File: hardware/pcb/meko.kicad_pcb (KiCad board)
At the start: 2 copper layers, 204 parts, among them IC1 MCP16502AB, IC2 MAYA-W386-00B, IC3 TAC5212, J1 Micro_SD_Card_Det1, J2 Micro_SD_Card_Det1, J3 USB_C_Receptacle_USB2.0_16P, J4 Conn_ARM_JTAG_SWD_10, J5 503480-1000, J6 PJ-342, J7 PJ-242, SW10 SW_Push, SW6 SW_Push, SW7 SW_Push, SW8 SW_Push, SW9 SW_Push, U1 SAMA7D65-4HB, U3 MAX17260, U4 BQ25640, U5 ECMF02-2AMX6, U6 TPS7A2033PDBV, U7 DRV2605LDGS, U8 MT41K256M16TW, Y1 32kHz768, Y2 24MHz, Y3 32kHz768

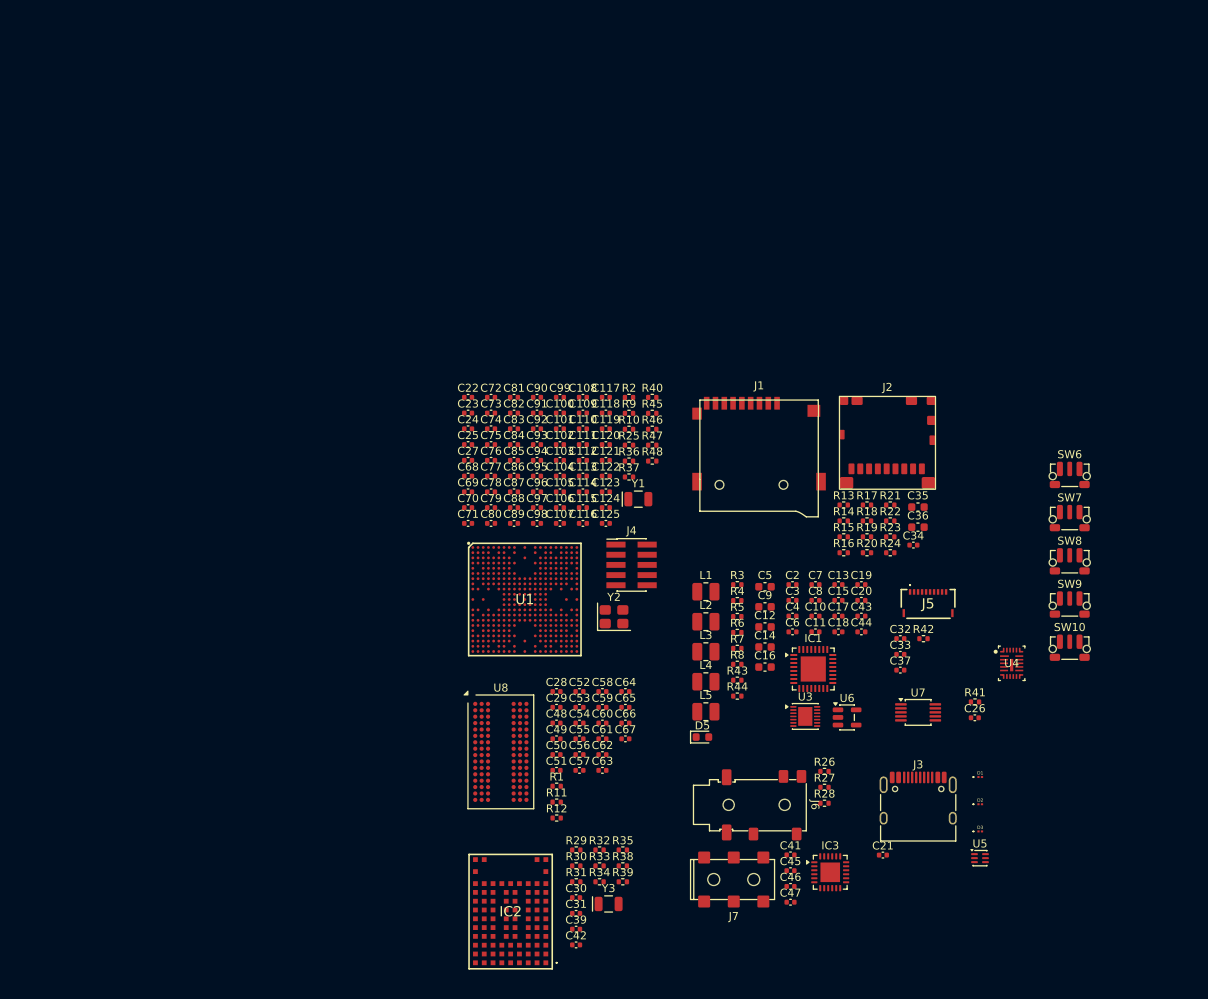
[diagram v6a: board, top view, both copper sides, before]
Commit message: mainboard: deleted footprint from pcb
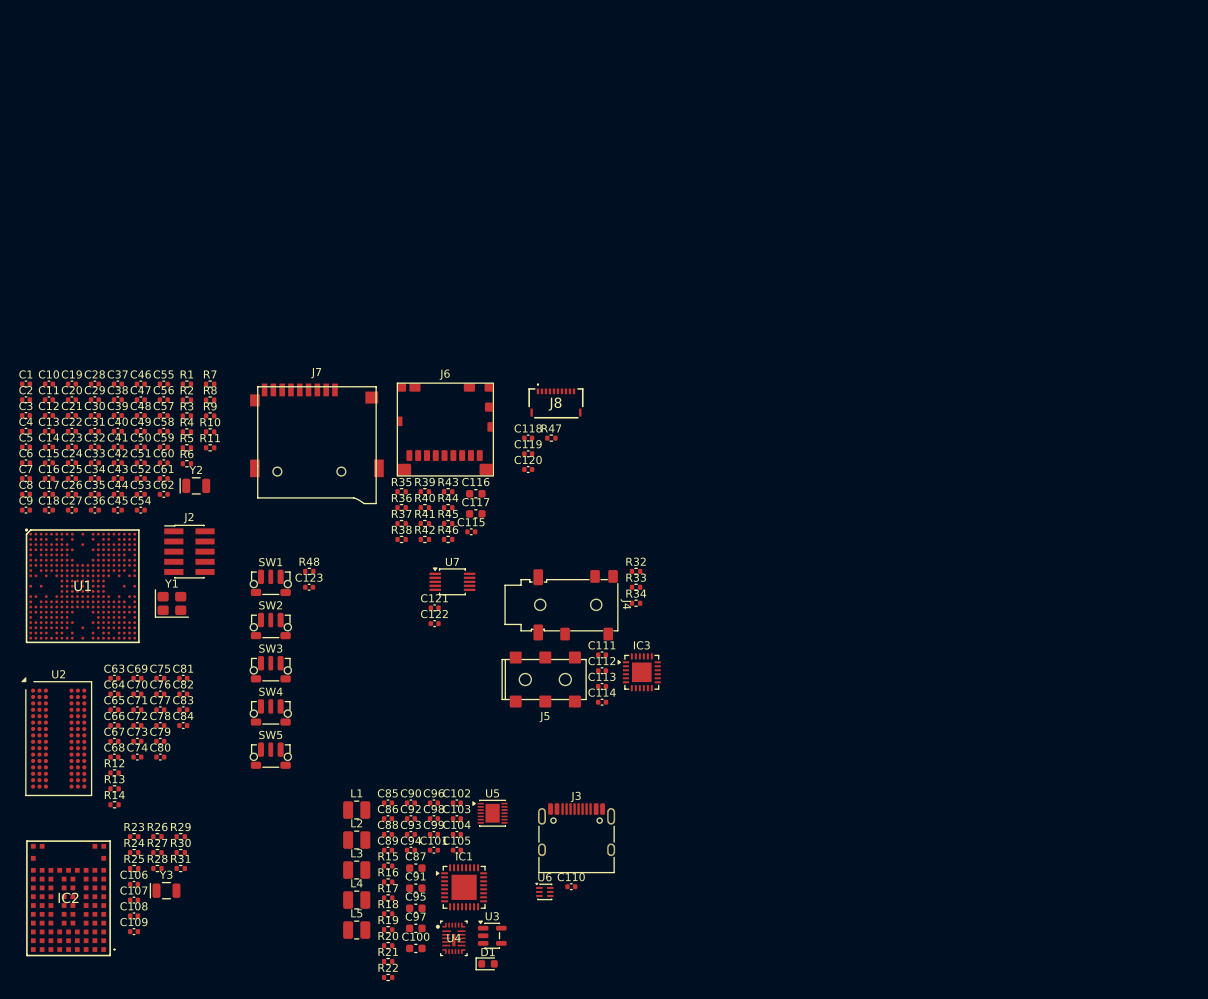
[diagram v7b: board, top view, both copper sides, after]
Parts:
- removed C124, C125: 100n, Capacitor_SMD:C_0402_1005Metric
- removed D2, D3: ESD441, ESD441DPLR:ESD441DPLR
- removed D5: LED, LED_SMD:LED_0603_1608Metric
- removed J1: Micro_SD_Card_Det1, PCM_ckl-connector:microSD_XYECONN_TF-015-ZYD9AH185
- removed SW10, SW6, SW7, SW8, SW9: SW_Push, Button_Switch_SMD:SW_Push_1P1T-MP_NO_Horizontal_Alps_SKRTLAE010
- removed U8: MT41K256M16TW, Package_BGA:Micron_FBGA-96_8x14mm_Layout9x16_P0.8mm
- added C1: 9p, Capacitor_SMD:C_0402_1005Metric, F.Cu at (14.6, 66.5)
- added C38: 100n, Capacitor_SMD:C_0402_1005Metric, F.Cu at (26.1, 68.5)
- added C40: 100n, Capacitor_SMD:C_0402_1005Metric, F.Cu at (26.1, 72.4)
- added J8: 503480-1000, 503480-1000:5034801000, F.Cu at (80.8, 68.9)
- added SW1: SW_Push, Button_Switch_SMD:SW_Push_1P1T-MP_NO_Horizontal_Alps_SKRTLAE010, F.Cu at (45.2, 91.5)
- added SW2: SW_Push, Button_Switch_SMD:SW_Push_1P1T-MP_NO_Horizontal_Alps_SKRTLAE010, F.Cu at (45.2, 96.9)
- added SW3: SW_Push, Button_Switch_SMD:SW_Push_1P1T-MP_NO_Horizontal_Alps_SKRTLAE010, F.Cu at (45.2, 102.3)
- added SW4: SW_Push, Button_Switch_SMD:SW_Push_1P1T-MP_NO_Horizontal_Alps_SKRTLAE010, F.Cu at (45.2, 107.7)
- added SW5: SW_Push, Button_Switch_SMD:SW_Push_1P1T-MP_NO_Horizontal_Alps_SKRTLAE010, F.Cu at (45.2, 113.1)
- added U2: MT41K256M16TW, Package_BGA:Micron_FBGA-96_8x14mm_Layout9x16_P0.8mm, F.Cu at (18.7, 110.8)
- C100: value 4u7 -> 22u; footprint Capacitor_SMD:C_0402_1005Metric -> Capacitor_SMD:C_0603_1608Metric
- C101, C103, C104, C105, C52, C53, C64, C66, C8, C93, C94, C96, C98: value 100n -> 4u7
- C102: value 100n -> 470n
- C106, C107, C110, C111, C112, C120, C121, C122, C85: value 100n -> 1u
- C108, C109: value 100n -> 9p
- C11, C13, C15, C17, C18, C19, C48, C67, C68, C83: value 4u7 -> 100n
- C113, C114, C86, C88: value 100n -> 10u
- C115: value 4u7 -> 10u
- C116, C117, C87, C91, C95, C97: value 100n -> 22u; footprint Capacitor_SMD:C_0402_1005Metric -> Capacitor_SMD:C_0603_1608Metric
- C119, C89, C90: value 4u7 -> 1u
- C12, C14, C16, C35, C36: value 22u -> 100n; footprint Capacitor_SMD:C_0603_1608Metric -> Capacitor_SMD:C_0402_1005Metric
- C2: value 1u -> 21pF
- C20, C34, C45, C46: value 10u -> 100n
- C21, C32, C37, C39, C41, C42, C43, C44, C47: value 1u -> 100n
- C22, C23, C27, C30, C31: value 9p -> 100n
- C24, C25: value 21pF -> 100n
- C3: value 10u -> 21pF
- C4: value 47n -> 100n
- C5: value 22u -> 9p; footprint Capacitor_SMD:C_0603_1608Metric -> Capacitor_SMD:C_0402_1005Metric
- C6: value 4u7 -> 9p
- C7: value 470n -> 4u7
- C9: value 22u -> 4u7; footprint Capacitor_SMD:C_0603_1608Metric -> Capacitor_SMD:C_0402_1005Metric
- C92: value 100n -> 47n
- D1: value ESD441 -> LED; footprint ESD441DPLR:ESD441DPLR -> LED_SMD:LED_0603_1608Metric
- J2: value Micro_SD_Card_Det1 -> Conn_ARM_JTAG_SWD_10; footprint PCM_ckl-connector:microSD_SOFNG_TF-008 -> Connector_PinHeader_1.27mm:PinHeader_2x05_P1.27mm_Vertical_SMD
- J4: value Conn_ARM_JTAG_SWD_10 -> PJ-342; footprint Connector_PinHeader_1.27mm:PinHeader_2x05_P1.27mm_Vertical_SMD -> PCM_ckl-connector:Jack_3.5mm_SHOUHAN_PJ-342
- J5: value 503480-1000 -> PJ-242; footprint 503480-1000:5034801000 -> PJ242:Jack_2.5mm_PJ242_6P_12x6.2x4mm_Horizontal
- J6: value PJ-342 -> Micro_SD_Card_Det1; footprint PCM_ckl-connector:Jack_3.5mm_SHOUHAN_PJ-342 -> PCM_ckl-connector:microSD_SOFNG_TF-008
- J7: value PJ-242 -> Micro_SD_Card_Det1; footprint PJ242:Jack_2.5mm_PJ242_6P_12x6.2x4mm_Horizontal -> PCM_ckl-connector:microSD_XYECONN_TF-015-ZYD9AH185
- R1, R2: value 240R -> 10k
- R10: value 4k02 -> 16k9
- R11: value 1k -> 16k9
- R13, R32: value 47k -> 1k
- R14: value 47k -> 240R
- R15, R16, R17, R21, R23, R30, R31: value 47k -> 10k
- R19: value 47k -> 1k5
- R20: value 47k -> 100R
- R22: value 47k -> 10m
- R25, R35, R36, R37, R38, R39, R41, R42, R43, R44: value 10k -> 47k
- R26, R27: value 100k -> 47k
- R28: value 1k -> 47k
- R3: value 100R -> 240R
- R33: value 47k -> 100k
- R34: value 10k -> 100k
- R4: value 10m -> 10k
- R45: value 16k9 -> 47k
- R46, R47, R48: value 16k9 -> 10k
- R5: value 1k5 -> 10k
- R6: value 10k -> 5k62
- R7: value 10k -> 4k02
- R8: value 10k -> 16k9
- R9: value 5k62 -> 16k9
- U3: value MAX17260 -> TPS7A2033PDBV; footprint Package_DFN_QFN:TDFN-14-1EP_3x3mm_P0.4mm_EP1.78x2.35mm -> Package_TO_SOT_SMD:SOT-23-5
- U5: value ECMF02-2AMX6 -> MAX17260; footprint Package_DFN_QFN:ST_UQFN-6L_1.5x1.7mm_P0.5mm -> Package_DFN_QFN:TDFN-14-1EP_3x3mm_P0.4mm_EP1.78x2.35mm
- U6: value TPS7A2033PDBV -> ECMF02-2AMX6; footprint Package_TO_SOT_SMD:SOT-23-5 -> Package_DFN_QFN:ST_UQFN-6L_1.5x1.7mm_P0.5mm
- Y1: value 32kHz768 -> 24MHz; footprint Crystal:Crystal_SMD_MicroCrystal_CC7V-T1A-2Pin_3.2x1.5mm -> Crystal:Crystal_SMD_3225-4Pin_3.2x2.5mm
- Y2: value 24MHz -> 32kHz768; footprint Crystal:Crystal_SMD_3225-4Pin_3.2x2.5mm -> Crystal:Crystal_SMD_MicroCrystal_CC7V-T1A-2Pin_3.2x1.5mm
- moved C26 116.3 mm to (20.3, 80.3)
- moved C21 115.3 mm to (20.3, 70.5)
- moved C37 104.1 mm to (26.1, 66.5)
- moved C32 103.5 mm to (23.2, 74.4)
- moved C33 103.5 mm to (23.2, 76.4)
- moved C36 102.9 mm to (23.2, 82.3)
- moved C35 102.9 mm to (23.2, 80.3)
- moved C46 102.7 mm to (28.9, 66.5)
- moved C47 102.7 mm to (28.9, 68.5)
- moved C34 102.7 mm to (23.2, 78.3)
- moved C20 101.8 mm to (20.3, 68.5)
- moved C19 101.8 mm to (20.3, 66.5)
- moved R23 101.7 mm to (28.1, 123.1)
- moved R24 101.7 mm to (28.1, 125.1)
- moved C13 100.5 mm to (17.5, 72.4)
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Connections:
- net /Touch Pad/SCL renamed /Touchpad/SCL
- net /Touch Pad/SDA renamed /Touchpad/SDA
- C10 pad 1: +VSYS -> +1V35_DDR
- C100 pad 1: +1V35_DDR -> +1V15_CPU
- C101 pad 1: +1V35_DDR -> +VSYS
- C102 pad 1: +1V35_DDR -> Net-(U5-REG)
- C103 pad 1: +1V35_DDR -> +VSYS
- C104 pad 1: +1V35_DDR -> +1V8_BATT_CPU
- C105 pad 1: +1V35_DDR -> +1V8
- C106 pad 1: +1V35_DDR -> GND
- C106 pad 2: GND -> +1V8
- C107 pad 1: +1V35_DDR -> +3V3
- C108 pad 1: +1V35_DDR -> Net-(IC2-SLP_XTAL_OUT)
- C109 pad 1: +1V35_DDR -> Net-(IC2-SLP_XTAL_IN)
- C11 pad 1: +VSYS -> +1V15_CORE
- C110 pad 1: +1V35_DDR -> GND
- C110 pad 2: GND -> VBUS
- C111 pad 1: +1V35_DDR -> GND
- C111 pad 2: GND -> Net-(IC3-DREG)
- C112 pad 1: +1V35_DDR -> GND
- C112 pad 2: GND -> Net-(IC3-VREF)
- C113 pad 1: +1V35_DDR -> GND
- C113 pad 2: GND -> +3V3
- C114 pad 1: +1V35_DDR -> GND
- C114 pad 2: GND -> +3V3_AVDD
- C115 pad 1: +1V8 -> +3V3
- C116 pad 1: +1V8 -> +3V3
- C117 pad 1: +1V8 -> +3V3
- C118 pad 1: +1V8 -> GND
- C118 pad 2: GND -> /Display/DISP
- C119 pad 1: +2V5 -> GND
- C119 pad 2: GND -> +3V3
- C12 pad 1: +1V35_DDR -> +1V15_CPU
- C120 pad 1: +2V5 -> GND
- C120 pad 2: GND -> +3V3
- C121 pad 1: +2V5 -> GND
- C121 pad 2: GND -> +3V3
- C122 pad 1: +2V5 -> GND
- C122 pad 2: GND -> Net-(U7-REG)
- C123 pad 1: +2V5 -> GND
- C123 pad 2: GND -> /Buttons/PWR
- C13 pad 1: +VSYS -> +3V3
- C14 pad 1: +1V15_CORE -> +1V35_DDR
- C15 pad 1: +VSYS -> +1V15_CORE
- C17 pad 1: +VSYS -> +3V3
- C18 pad 1: +1V8_BATT_CPU -> +1V35_DDR
- C19 pad 1: +1V8 -> +1V15_CORE
- C2 pad 1: VBUS -> Net-(U1SYS-XIN)
- C20 pad 1: +VSYS -> +1V15_CPU
- C21 pad 1: GND -> +3V3
- C21 pad 2: VBUS -> GND
- C22 pad 1: Net-(U1SYS-XIN32) -> +1V35_DDR
- C23 pad 1: Net-(U1SYS-XOUT32) -> +1V15_CORE
- C24 pad 1: Net-(U1SYS-XIN) -> +1V15_CPU
- C25 pad 1: Net-(U1SYS-XOUT) -> +3V3
- C26 pad 1: GND -> +1V35_DDR
- C26 pad 2: /Buttons/PWR -> GND
- C27 pad 1: Net-(U1PERIs-HHSRTUNE) -> +1V15_CORE
- C28 pad 1: DDR_VREF -> +1V15_CPU
- C28 pad 2: +1V2_DDR -> GND
- C29 pad 1: GND -> +3V3
- C29 pad 2: DDR_VREF -> GND
- C3 pad 1: Net-(U4-PMID) -> Net-(U1SYS-XOUT)
- C30 pad 1: Net-(IC2-SLP_XTAL_OUT) -> +1V35_DDR
- C31 pad 1: Net-(IC2-SLP_XTAL_IN) -> +1V15_CORE
- C32 pad 1: GND -> +3V3
- C32 pad 2: +3V3 -> GND
- C33 pad 1: GND -> +1V35_DDR
- C33 pad 2: /Display/DISP -> GND
- C34 pad 1: +3V3 -> +1V15_CORE
- C36 pad 1: +3V3 -> +1V35_DDR
- C37 pad 1: GND -> +1V15_CORE
- C37 pad 2: +3V3 -> GND
- C39 pad 1: +3V3 -> +1V35_DDR
- C4 pad 1: Net-(U4-BTST) -> /SAMA7/VBAT
- C4 pad 2: Net-(U4-SW) -> GND
- C41 pad 1: GND -> +1V35_DDR
- C41 pad 2: Net-(IC3-DREG) -> GND
- C42 pad 1: GND -> +1V15_CORE
- C42 pad 2: +1V8 -> GND
- C43 pad 1: +3V3 -> +1V35_DDR
- C44 pad 1: +3V3_AVDD -> +1V15_CORE
- C45 pad 1: GND -> +1V35_DDR
- C45 pad 2: +3V3 -> GND
- C46 pad 1: GND -> +1V15_CORE
- C46 pad 2: +3V3_AVDD -> GND
- C47 pad 1: GND -> +1V35_DDR
- C47 pad 2: Net-(IC3-VREF) -> GND
- C48 pad 1: +1V2_DDR -> +1V15_CORE
- C5 pad 1: +VSYS -> Net-(U1SYS-XIN32)
- C50 pad 1: +1V35_DDR -> +1V15_CORE
- C52 pad 1: +1V35_DDR -> +1V8
- C53 pad 1: +1V35_DDR -> +2V5
- C54 pad 1: +1V35_DDR -> +1V8
- C55 pad 1: +1V35_DDR -> +2V5
- C56 pad 1: +1V35_DDR -> +1V8
- C57 pad 1: +1V35_DDR -> +2V5
- C58 pad 1: +1V35_DDR -> +1V8
- C59 pad 1: +1V35_DDR -> +2V5
- C6 pad 1: Net-(U4-REGN) -> Net-(U1SYS-XOUT32)
- C60 pad 1: +1V35_DDR -> +2V5
- C61 pad 1: +1V35_DDR -> +2V5
- C62 pad 1: +1V35_DDR -> +2V5
- C63 pad 1: +1V35_DDR -> DDR_VREF
- C63 pad 2: GND -> +1V2_DDR
- C64 pad 1: +1V35_DDR -> +1V2_DDR
- C65 pad 1: +1V35_DDR -> GND
- C65 pad 2: GND -> DDR_VREF
- C68 pad 1: +1V15_CORE -> +1V35_DDR
- C69 pad 1: +1V15_CORE -> +1V35_DDR
- C7 pad 1: Net-(U3-REG) -> +1V15_CORE
- C70 pad 1: +1V15_CORE -> +1V35_DDR
- C71 pad 1: +1V15_CORE -> +1V35_DDR
- C72 pad 1: +1V15_CORE -> +1V35_DDR
- C73 pad 1: +1V15_CORE -> +1V35_DDR
- C74 pad 1: +1V15_CORE -> +1V35_DDR
- C75 pad 1: +1V15_CORE -> +1V35_DDR
- C76 pad 1: +1V15_CORE -> +1V35_DDR
- C77 pad 1: +1V15_CORE -> +1V35_DDR
- C78 pad 1: +1V15_CORE -> +1V35_DDR
- C79 pad 1: +1V15_CORE -> +1V35_DDR
- C8 pad 1: +BATT -> +1V15_CPU
- C80 pad 1: +1V15_CORE -> +1V35_DDR
- C81 pad 1: +1V15_CORE -> +1V35_DDR
- C82 pad 1: +1V15_CORE -> +1V35_DDR
- C83 pad 1: +1V15_CPU -> +1V35_DDR
- C84 pad 1: +1V15_CPU -> +1V35_DDR
- C85 pad 1: +1V15_CPU -> VBUS
- C86 pad 1: +1V15_CPU -> Net-(U4-PMID)
- C87 pad 1: +1V15_CPU -> +VSYS
- C88 pad 1: +1V15_CPU -> +VSYS
- C89 pad 1: unconnected-(C89-Pad1) -> +3V3
- C89 pad 2: unconnected-(C89-Pad2) -> GND
- C90 pad 1: +3V3 -> +3V3_AVDD
- C92 pad 1: +3V3 -> Net-(U4-BTST)
- C92 pad 2: GND -> Net-(U4-SW)
- C93 pad 1: +3V3 -> +VSYS
- C94 pad 1: +3V3 -> Net-(U4-REGN)
- C95 pad 1: +3V3 -> +1V35_DDR
- C96 pad 1: +3V3 -> +VSYS
- C97 pad 1: +3V3 -> +1V15_CORE
- C98 pad 1: +3V3 -> +VSYS
- C99 pad 1: /SAMA7/VBAT -> +BATT
- D1 pad 1: /Power/CC1 -> Net-(D1-K)
- D1 pad 2: GND -> +VSYS
- J2 pad 1: /SAMA7/BOOT.DAT2 -> +3V3
- J2 pad 10: (no net) -> /Power/~{RST}
- J2 pad 2: /SAMA7/BOOT.DAT3 -> /SAMA7/TMS
- J2 pad 3: /SAMA7/BOOT.CMD -> GND
- J2 pad 4: +3V3 -> /SAMA7/TCK
- J2 pad 5: /SAMA7/BOOT.CK -> GND
- J2 pad 6: GND -> /SAMA7/TDO
- J2 pad 7: /SAMA7/BOOT.DAT0 -> unconnected-(J2-KEY-Pad7)
- J2 pad 8: /SAMA7/BOOT.DAT1 -> /SAMA7/TDI
- J2 pad 9: /SAMA7/BOOT.CD -> GND
- J4 pad 1: +3V3 -> (no net)
- J4 pad 2: /SAMA7/TMS -> (no net)
- J4 pad 3: GND -> (no net)
- J4 pad 4: /SAMA7/TCK -> (no net)
- L1 pad 1: Net-(U4-SW) -> Net-(IC1-SW1)
- L1 pad 2: +VSYS -> +3V3
- L2 pad 1: Net-(IC1-SW1) -> Net-(U4-SW)
- L2 pad 2: +3V3 -> +VSYS
- R1 pad 1: Net-(U8-ZQ) -> /Audio/SCL
- R1 pad 2: GND -> +3V3
- R10 pad 1: Net-(U1PERIs-MIPI_REXT) -> GND
- R10 pad 2: GND -> Net-(U1PERIs-SDMMC2_CAL)
- R11 pad 1: +1V2_DDR -> GND
- R11 pad 2: DDR_VREF -> Net-(U1PERIs-QSPI0_CAL)
- R12 pad 1: DDR_VREF -> +1V2_DDR
- R12 pad 2: GND -> DDR_VREF
- R13 pad 1: +3V3 -> DDR_VREF
- R13 pad 2: /SAMA7/BOOT.DAT2 -> GND
- R14 pad 1: +3V3 -> Net-(U2-ZQ)
- R14 pad 2: /SAMA7/BOOT.DAT3 -> GND
- R15 pad 1: +3V3 -> /Power/~{WKUP}
- R15 pad 2: /SAMA7/BOOT.CMD -> +VSYS
- R16 pad 1: +3V3 -> /Power/~{RST}
- R16 pad 2: /SAMA7/BOOT.DAT0 -> +3V3
- R17 pad 1: +3V3 -> /Power/~{INT}
- R17 pad 2: /SAMA7/BOOT.DAT1 -> +3V3
- R18 pad 1: +3V3 -> /Power/CHG_~{INT}
- R18 pad 2: /SAMA7/BOOT.CD -> +3V3
- R19 pad 1: +3V3 -> Net-(U4-~{PG})
- R19 pad 2: /SAMA7/EXT.DAT2 -> Net-(D1-K)
- R2 pad 1: Net-(U1DDR-DDR_ZQ) -> /Audio/SDA
- R2 pad 2: GND -> +3V3
- R20 pad 1: +3V3 -> Net-(U4-BATP)
- R20 pad 2: /SAMA7/EXT.DAT3 -> +BATT
- R21 pad 1: +3V3 -> /Power/FUEL_~{INT}
- R21 pad 2: /SAMA7/EXT.CMD -> +3V3
- R22 pad 1: +3V3 -> Net-(BT1--)
- R22 pad 2: /SAMA7/EXT.DAT0 -> GND
- R23 pad 1: +3V3 -> GND
- R23 pad 2: /SAMA7/EXT.DAT1 -> /SAMA7/BT.DEV_WAKE
- R24 pad 1: +3V3 -> GND
- R24 pad 2: /SAMA7/EXT.CD -> /SAMA7/BT.HOST_WAKE
- R25 pad 1: /SAMA7/TOUCH.SDA -> +3V3
- R25 pad 2: +3V3 -> /SAMA7/WIFI.CMD
- R26 pad 1: GND -> +3V3
- R26 pad 2: /Audio/~{DET}_3.5mm -> /SAMA7/WIFI.DAT0
- R27 pad 1: GND -> +3V3
- R27 pad 2: /Audio/~{DET}_2.5mm -> /SAMA7/WIFI.DAT1
- R28 pad 1: /Audio/MIC -> +3V3
- R28 pad 2: +MICBIAS -> /SAMA7/WIFI.DAT2
- R29 pad 2: /SAMA7/WIFI.CMD -> /SAMA7/WIFI.DAT3
- R3 pad 1: Net-(U4-BATP) -> Net-(U1DDR-DDR_ZQ)
- R3 pad 2: +BATT -> GND
- R30 pad 1: +3V3 -> GND
- R30 pad 2: /SAMA7/WIFI.DAT0 -> /SAMA7/WL.HOST_WAKE
- R31 pad 1: +3V3 -> GND
- R31 pad 2: /SAMA7/WIFI.DAT1 -> /SAMA7/WL.DEV_WAKE
- R32 pad 1: +3V3 -> /Audio/MIC
- R32 pad 2: /SAMA7/WIFI.DAT2 -> +MICBIAS
- R33 pad 1: +3V3 -> GND
- R33 pad 2: /SAMA7/WIFI.DAT3 -> /Audio/~{DET}_3.5mm
- R34 pad 2: /SAMA7/WL.HOST_WAKE -> /Audio/~{DET}_2.5mm
- R35 pad 1: GND -> +3V3
- R35 pad 2: /SAMA7/WL.DEV_WAKE -> /SAMA7/BOOT.DAT2
- R36 pad 1: /SAMA7/TOUCH.SCL -> +3V3
- R36 pad 2: +3V3 -> /SAMA7/BOOT.DAT3
- R37 pad 1: /Audio/SCL -> +3V3
- R37 pad 2: +3V3 -> /SAMA7/BOOT.CMD
- R38 pad 1: GND -> +3V3
- R38 pad 2: /SAMA7/BT.DEV_WAKE -> /SAMA7/BOOT.DAT0
- R39 pad 1: GND -> +3V3
- R39 pad 2: /SAMA7/BT.HOST_WAKE -> /SAMA7/BOOT.DAT1
- R4 pad 1: Net-(BT1--) -> /SAMA7/TOUCH.SCL
- R4 pad 2: GND -> +3V3
- R40 pad 1: /Audio/SDA -> +3V3
- R40 pad 2: +3V3 -> /SAMA7/BOOT.CD
- R41 pad 1: Net-(R41-Pad1) -> +3V3
- R41 pad 2: /Buttons/PWR -> /SAMA7/EXT.DAT2
- R42 pad 1: GND -> +3V3
- R42 pad 2: /Display/DISP -> /SAMA7/EXT.DAT3
- R43 pad 1: /Power/FUEL_~{INT} -> +3V3
- R43 pad 2: +3V3 -> /SAMA7/EXT.CMD
- R44 pad 1: /Power/CHG_~{INT} -> +3V3
- R44 pad 2: +3V3 -> /SAMA7/EXT.DAT0
- R45 pad 1: GND -> +3V3
- R45 pad 2: Net-(U1PERIs-SDMMC0_CAL) -> /SAMA7/EXT.DAT1
- R46 pad 1: GND -> +3V3
- R46 pad 2: Net-(U1PERIs-SDMMC1_CAL) -> /SAMA7/EXT.CD
- R47 pad 2: Net-(U1PERIs-SDMMC2_CAL) -> /Display/DISP
- R48 pad 1: GND -> Net-(R48-Pad1)
- R48 pad 2: Net-(U1PERIs-QSPI0_CAL) -> /Buttons/PWR
- R5 pad 1: Net-(U4-~{PG}) -> /SAMA7/TOUCH.SDA
- R5 pad 2: Net-(D5-K) -> +3V3
- R6 pad 1: /Power/~{INT} -> GND
- R6 pad 2: +3V3 -> Net-(U1PERIs-HHSRTUNE)
- R7 pad 1: /Power/~{RST} -> Net-(U1PERIs-MIPI_REXT)
- R7 pad 2: +3V3 -> GND
- R8 pad 1: /Power/~{WKUP} -> GND
- R8 pad 2: +VSYS -> Net-(U1PERIs-SDMMC0_CAL)
- R9 pad 2: Net-(U1PERIs-HHSRTUNE) -> Net-(U1PERIs-SDMMC1_CAL)
- U1 pad AA16: /SAMA7/TOUCH_~{RST} -> unconnected-(U1GPIO C&D&E-PE8-PadAA16)
- U1 pad AA19: /SAMA7/HAPT_~{INT} -> unconnected-(U1GPIO C&D&E-PE10-PadAA19)
- U1 pad AA20: /Display/SCS -> unconnected-(U1GPIO A&B-PA23-PadAA20)
- U1 pad W19: unconnected-(U1GPIO A&B-PA21-PadW19) -> /Display/SCS
- U3 pad 1: +BATT -> +3V3
- U3 pad 2: unconnected-(U3-NC-Pad2) -> GND
- U3 pad 3: unconnected-(U3-NC-Pad3) -> +3V3
- U3 pad 5: unconnected-(U3-NC-Pad5) -> +3V3_AVDD
- U5 pad 1: /USB/DIRTY_D+ -> +BATT
- U5 pad 2: /USB/DIRTY_D- -> unconnected-(U5-NC-Pad2)
- U5 pad 3: GND -> unconnected-(U5-NC-Pad3)
- U5 pad 5: /SAMA7/D- -> unconnected-(U5-NC-Pad5)
- U5 pad 6: /SAMA7/D+ -> +BATT
- U6 pad 1: +3V3 -> /USB/DIRTY_D+
- U6 pad 2: GND -> /USB/DIRTY_D-
- U6 pad 3: +3V3 -> GND
- U6 pad 5: +3V3_AVDD -> /SAMA7/D-
- U7 pad 1: unconnected-(U7-REG-Pad1) -> Net-(U7-REG)
- U7 pad 10: Net-(U7-VDD) -> +3V3
- U7 pad 4: /SAMA7/HAPT_~{INT} -> GND
- U7 pad 6: Net-(U7-VDD) -> +3V3
- U7 pad 7: unconnected-(U7-OUT+-Pad7) -> Net-(U7-OUT+)
- U7 pad 9: unconnected-(U7-OUT--Pad9) -> Net-(U7-OUT-)
- Y1 pad 1: Net-(U1SYS-XOUT32) -> Net-(U1SYS-XIN)
- Y1 pad 2: Net-(U1SYS-XIN32) -> GND
- Y2 pad 1: Net-(U1SYS-XIN) -> Net-(U1SYS-XOUT32)
- Y2 pad 2: GND -> Net-(U1SYS-XIN32)

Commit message: assigned missing footprints
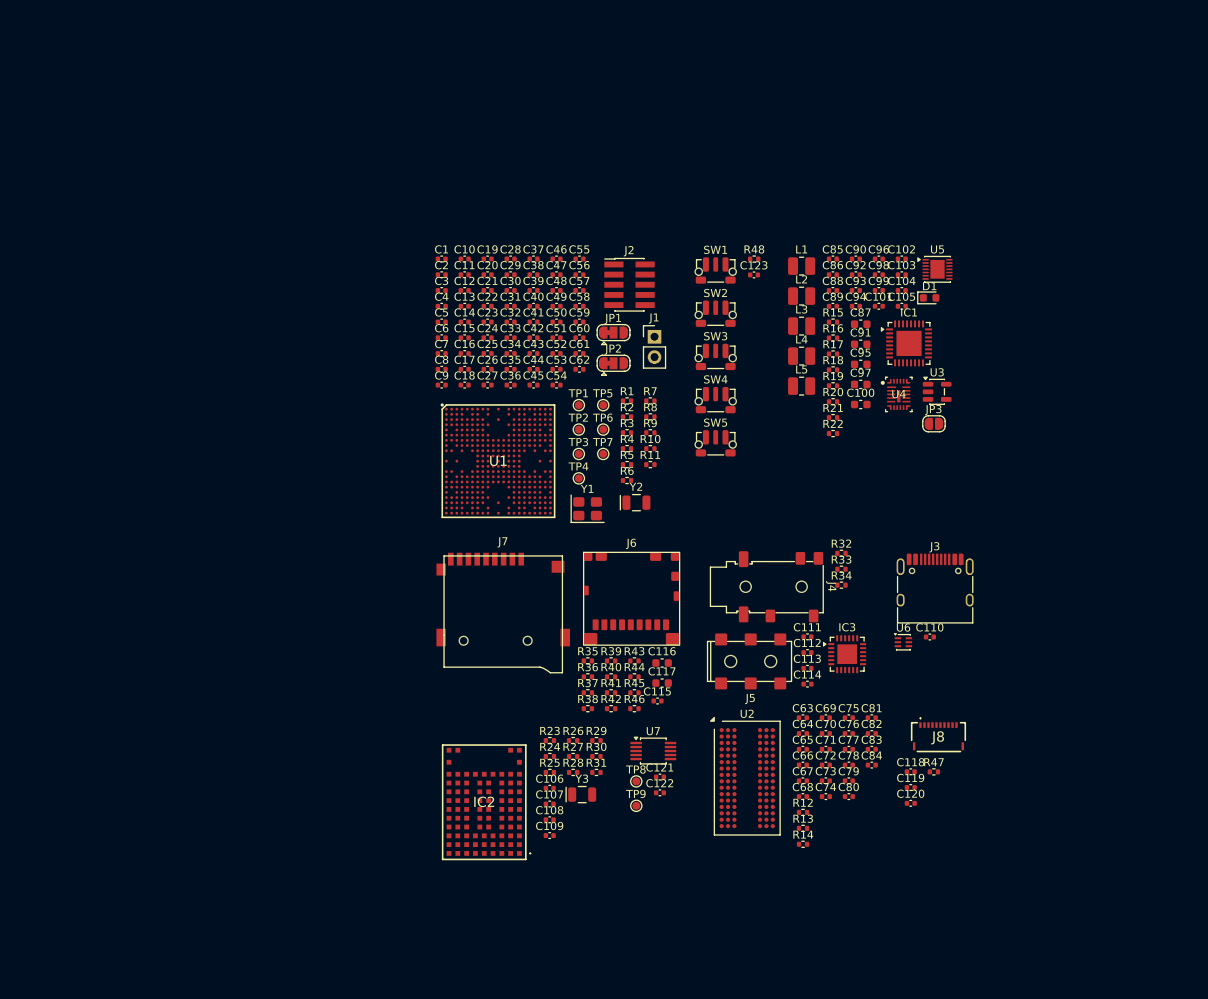
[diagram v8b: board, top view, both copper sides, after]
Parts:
- added J1: Conn_01x02_Pin, Connector_PinHeader_2.54mm:PinHeader_1x02_P2.54mm_Vertical, F.Cu at (93.2, 60.6)
- added JP1: JTAGSEL, Jumper:SolderJumper-3_P1.3mm_Bridged12_RoundedPad1.0x1.5mm, F.Cu at (88.0, 60.1)
- added JP2: VBATSEL, Jumper:SolderJumper-3_P1.3mm_Bridged12_RoundedPad1.0x1.5mm, F.Cu at (88.0, 63.9)
- added JP3: SolderJumper_2_Open, Jumper:SolderJumper-2_P1.3mm_Open_RoundedPad1.0x1.5mm, F.Cu at (128.1, 71.5)
- added TP1: ~{TRST}, TestPoint:TestPoint_Pad_D1.0mm, F.Cu at (83.7, 69.2)
- added TP2: ~{TRST}, TestPoint:TestPoint_Pad_D1.0mm, F.Cu at (83.7, 72.2)
- added TP3: ~{RST_OUT}, TestPoint:TestPoint_Pad_D1.0mm, F.Cu at (83.7, 75.3)
- added TP4: ~{TRST}, TestPoint:TestPoint_Pad_D1.0mm, F.Cu at (83.7, 78.3)
- added TP5: ~{TRST}, TestPoint:TestPoint_Pad_D1.0mm, F.Cu at (86.7, 69.2)
- added TP6: ~{TRST}, TestPoint:TestPoint_Pad_D1.0mm, F.Cu at (86.7, 72.2)
- added TP7: ~{TRST}, TestPoint:TestPoint_Pad_D1.0mm, F.Cu at (86.7, 75.3)
- added TP8: HAPT+, TestPoint:TestPoint_Pad_D1.0mm, F.Cu at (90.9, 116.2)
- added TP9: HAPT-, TestPoint:TestPoint_Pad_D1.0mm, F.Cu at (90.9, 119.2)
- moved D1 99.9 mm to (127.5, 55.7)
- moved C87 87.8 mm to (118.9, 59.0)
- moved C90 87.8 mm to (118.3, 50.9)
- moved C92 87.8 mm to (118.3, 52.9)
- moved C97 87.8 mm to (118.9, 66.6)
- moved L1 87.8 mm to (111.5, 51.8)
- moved L2 87.8 mm to (111.5, 55.5)
- moved L3 87.8 mm to (111.5, 59.3)
- moved U4 87.8 mm to (123.7, 67.8)
- moved C100 87.8 mm to (118.9, 69.1)
- moved C101 87.8 mm to (121.2, 56.8)
- moved C102 87.8 mm to (124.1, 50.9)
- moved C103 87.8 mm to (124.1, 52.9)
- moved C104 87.8 mm to (124.1, 54.8)
- moved C105 87.8 mm to (124.1, 56.8)
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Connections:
- net DDR_VREF renamed /DDR/DDR_VREF
